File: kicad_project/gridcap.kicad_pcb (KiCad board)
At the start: 2 copper layers, 68 parts

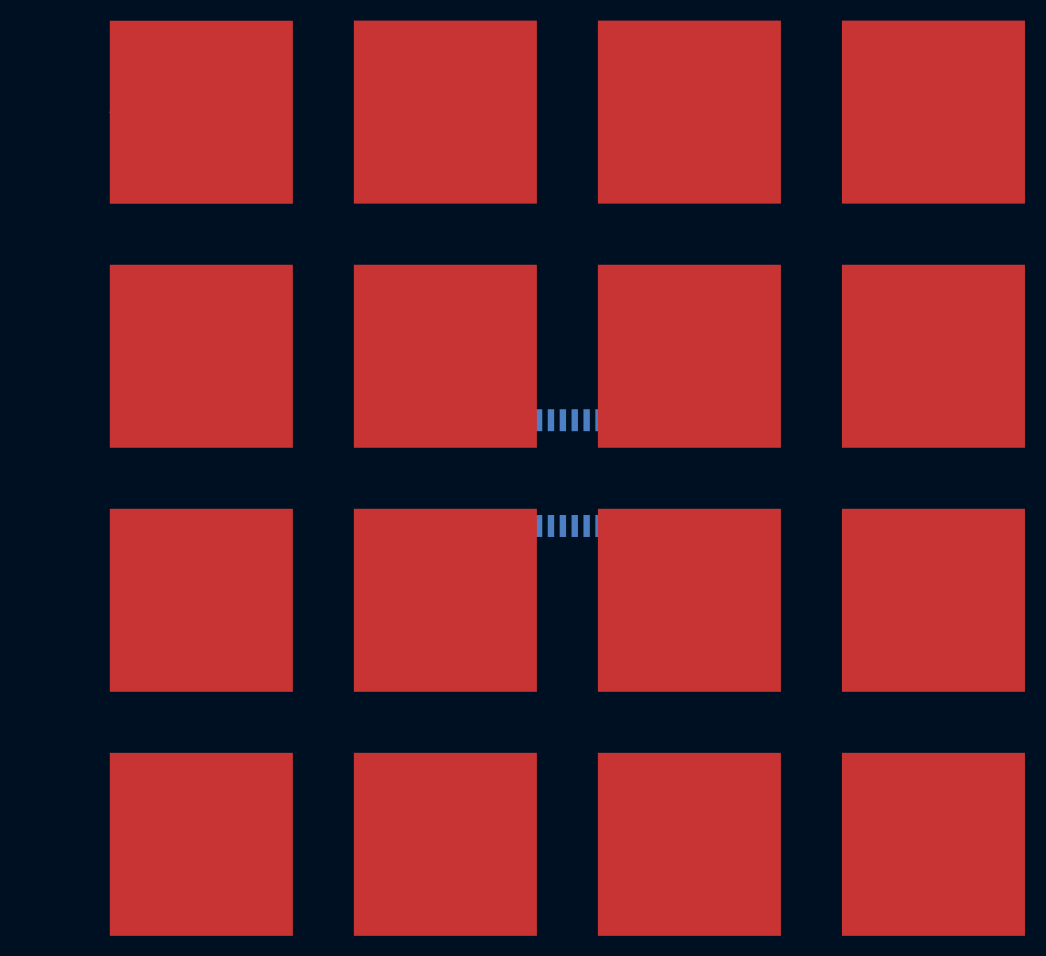
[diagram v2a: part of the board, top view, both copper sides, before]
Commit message: Route one mux on pcb
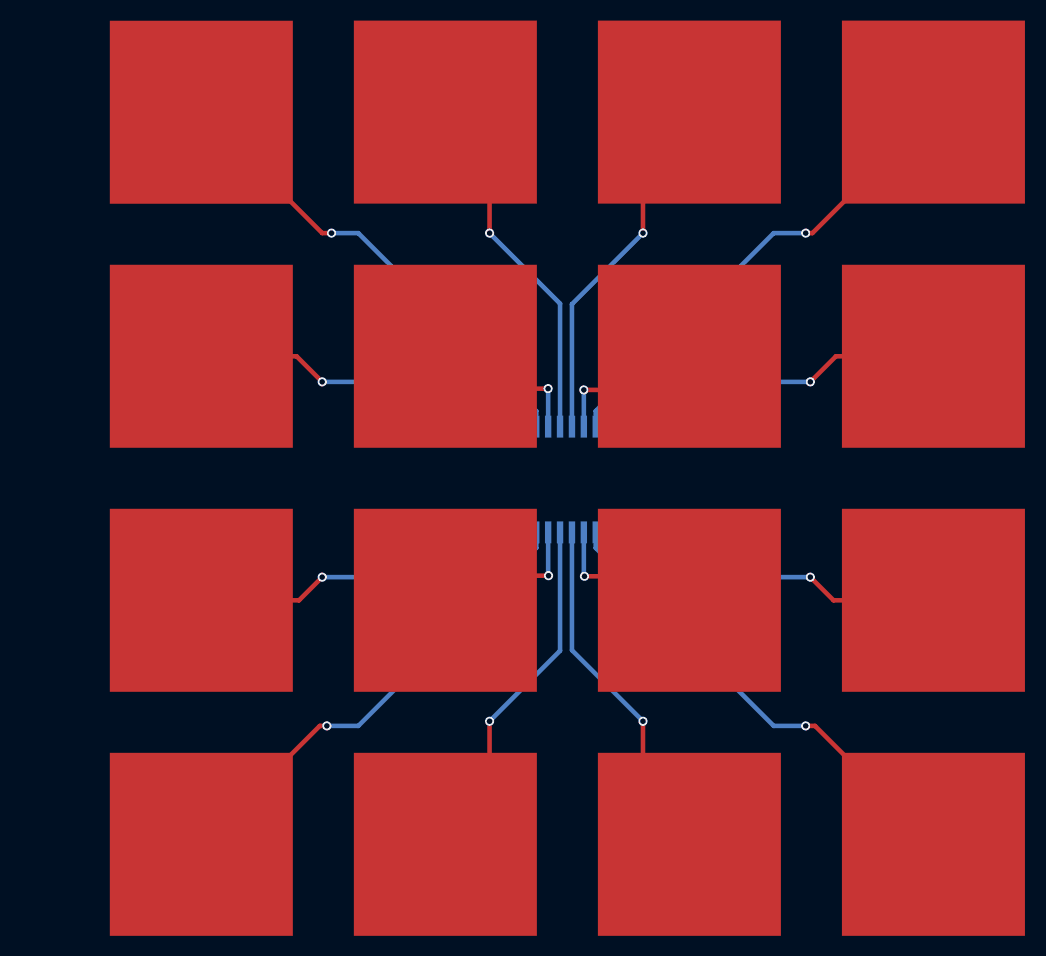
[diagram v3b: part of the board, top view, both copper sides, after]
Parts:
- moved MUX1 0.61 mm to (185.7, 73.4)
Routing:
- net Net-(MUX1-Y1): track 0.00 -> 26.1 mm, vias 0 -> 1
- net Net-(MUX1-Y14): track 0.00 -> 26.0 mm, vias 0 -> 1
- net Net-(MUX1-Y9): track 0.00 -> 25.9 mm, vias 0 -> 1
- net Net-(MUX1-Y6): track 5.00 -> 25.9 mm, vias 0 -> 1
- net Net-(MUX1-Y0): track 0.00 -> 19.9 mm, vias 0 -> 1
- net Net-(MUX1-Y3): track 0.00 -> 19.8 mm, vias 0 -> 1
- net Net-(MUX1-Y15): track 0.00 -> 19.8 mm, vias 0 -> 1
- net Net-(MUX1-Y4): track 0.00 -> 19.8 mm, vias 0 -> 1
- net Net-(MUX1-Y7): track 0.00 -> 19.7 mm, vias 0 -> 1
- net Net-(MUX1-Y12): track 0.00 -> 19.7 mm, vias 0 -> 1
- net Net-(MUX1-Y8): track 0.00 -> 19.7 mm, vias 0 -> 1
- net Net-(MUX1-Y11): track 0.00 -> 19.6 mm, vias 0 -> 1
- net Net-(MUX1-Y13): track 0.00 -> 8.69 mm, vias 0 -> 1
- net Net-(MUX1-Y10): track 0.00 -> 8.57 mm, vias 0 -> 1
- net Net-(MUX1-Y2): track 0.00 -> 8.54 mm, vias 0 -> 1
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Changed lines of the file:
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@@
   )
   (footprint "gridcap_footprints:74HC4067PW-Q100J" (layer "B.Cu")
-    (at 185.177 73.056)
+    (at 185.674 73.406)
     (descr "TSSOP24")
     (property "Sheetfile" "gridcap.kicad_sch")
@@
       (net 122 "unconnected-(MUX1-Vcc-Pad24)") (pinfunction "Vcc") (pintype "power_in") (thermal_bridge_angle 45))
   )
-  (segment (start 165.1 53.34) (end 160.1 53.34) (width 0) (layer "F.Cu") (net 3))
+  (segment (start 170.305 66.673) (end 165.1 66.673) (width 0.25) (layer "F.Cu") (net 2))
+  (segment (start 171.704 68.072) (end 170.305 66.673) (width 0.25) (layer "F.Cu") (net 2))
+  (via (at 171.704 68.072) (size 0.5) (drill 0.3) (layers "F.Cu" "B.Cu") (net 2))
+  (segment (start 182.749 69.666) (end 181.155 68.072) (width 0.25) (layer "B.Cu") (net 2))
+  (segment (start 181.155 68.072) (end 171.704 68.072) (width 0.25) (layer "B.Cu") (net 2))
+  (segment (start 182.749 70.516) (end 182.749 69.666) (width 0.25) (layer "B.Cu") (net 2))
+  (segment (start 171.704 59.944) (end 165.1 53.34) (width 0.25) (layer "F.Cu") (net 3))
+  (segment (start 172.212 59.944) (end 171.704 59.944) (width 0.25) (layer "F.Cu") (net 3))
+  (via (at 172.212 59.944) (size 0.5) (drill 0.3) (layers "F.Cu" "B.Cu") (net 3))
+  (segment (start 183.399 70.516) (end 183.399 69.666) (width 0.25) (layer "B.Cu") (net 3))
+  (segment (start 173.677 59.944) (end 172.212 59.944) (width 0.25) (layer "B.Cu") (net 3))
+  (segment (start 183.399 69.666) (end 173.677 59.944) (width 0.25) (layer "B.Cu") (net 3))
+  (segment (start 184.044991 68.441875) (end 180.201875 68.441875) (width 0.25) (layer "F.Cu") (net 4))
+  (segment (start 180.201875 68.441875) (end 178.433 66.673) (width 0.25) (layer "F.Cu") (net 4))
+  (via (at 184.044991 68.441875) (size 0.5) (drill 0.3) (layers "F.Cu" "B.Cu") (net 4))
+  (segment (start 184.049 68.445884) (end 184.044991 68.441875) (width 0.25) (layer "B.Cu") (net 4))
+  (segment (start 184.049 70.516) (end 184.049 68.445884) (width 0.25) (layer "B.Cu") (net 4))
+  (segment (start 180.848 55.7478) (end 178.433 53.3328) (width 0.25) (layer "F.Cu") (net 5))
+  (segment (start 180.848 59.944) (end 180.848 55.7478) (width 0.25) (layer "F.Cu") (net 5))
+  (via (at 180.848 59.944) (size 0.5) (drill 0.3) (layers "F.Cu" "B.Cu") (net 5))
+  (segment (start 184.699 63.795) (end 180.848 59.944) (width 0.25) (layer "B.Cu") (net 5))
+  (segment (start 184.699 70.516) (end 184.699 63.795) (width 0.25) (layer "B.Cu") (net 5))
+  (segment (start 189.23 55.8688) (end 191.766 53.3328) (width 0.25) (layer "F.Cu") (net 6))
+  (segment (start 189.23 59.944) (end 189.23 55.8688) (width 0.25) (layer "F.Cu") (net 6))
+  (via (at 189.23 59.944) (size 0.5) (drill 0.3) (layers "F.Cu" "B.Cu") (net 6))
+  (segment (start 185.349 63.825) (end 189.23 59.944) (width 0.25) (layer "B.Cu") (net 6))
+  (segment (start 185.349 70.516) (end 185.349 63.825) (width 0.25) (layer "B.Cu") (net 6))
+  (segment (start 189.927805 68.511195) (end 191.766 66.673) (width 0.25) (layer "F.Cu") (net 7))
+  (segment (start 185.997491 68.511195) (end 189.927805 68.511195) (width 0.25) (layer "F.Cu") (net 7))
+  (via (at 185.997491 68.511195) (size 0.5) (drill 0.3) (layers "F.Cu" "B.Cu") (net 7))
+  (segment (start 185.999 68.512704) (end 185.997491 68.511195) (width 0.25) (layer "B.Cu") (net 7))
+  (segment (start 185.999 70.516) (end 185.999 68.512704) (width 0.25) (layer "B.Cu") (net 7))
+  (segment (start 198.4878 59.944) (end 205.099 53.3328) (width 0.25) (layer "F.Cu") (net 8))
+  (segment (start 198.12 59.944) (end 198.4878 59.944) (width 0.25) (layer "F.Cu") (net 8))
+  (via (at 198.12 59.944) (size 0.5) (drill 0.3) (layers "F.Cu" "B.Cu") (net 8))
+  (segment (start 196.371 59.944) (end 198.12 59.944) (width 0.25) (layer "B.Cu") (net 8))
+  (segment (start 186.649 69.666) (end 196.371 59.944) (width 0.25) (layer "B.Cu") (net 8))
+  (segment (start 186.649 70.516) (end 186.649 69.666) (width 0.25) (layer "B.Cu") (net 8))
+  (segment (start 199.773 66.673) (end 205.099 66.673) (width 0.25) (layer "F.Cu") (net 9))
+  (segment (start 198.374 68.072) (end 199.773 66.673) (width 0.25) (layer "F.Cu") (net 9))
+  (via (at 198.374 68.072) (size 0.5) (drill 0.3) (layers "F.Cu" "B.Cu") (net 9))
+  (segment (start 187.299 69.666) (end 188.893 68.072) (width 0.25) (layer "B.Cu") (net 9))
+  (segment (start 188.893 68.072) (end 198.374 68.072) (width 0.25) (layer "B.Cu") (net 9))
+  (segment (start 187.299 70.516) (end 187.299 69.666) (width 0.25) (layer "B.Cu") (net 9))
+  (segment (start 199.64 80.006) (end 205.099 80.006) (width 0.25) (layer "F.Cu") (net 15))
+  (segment (start 198.374 78.74) (end 199.64 80.006) (width 0.25) (layer "F.Cu") (net 15))
+  (via (at 198.374 78.74) (size 0.5) (drill 0.3) (layers "F.Cu" "B.Cu") (net 15))
+  (segment (start 188.893 78.74) (end 198.374 78.74) (width 0.25) (layer "B.Cu") (net 15))
+  (segment (start 187.299 77.146) (end 188.893 78.74) (width 0.25) (layer "B.Cu") (net 15))
+  (segment (start 187.299 76.296) (end 187.299 77.146) (width 0.25) (layer "B.Cu") (net 15))
+  (segment (start 198.628 86.868) (end 205.099 93.339) (width 0.25) (layer "F.Cu") (net 16))
+  (segment (start 198.12 86.868) (end 198.628 86.868) (width 0.25) (layer "F.Cu") (net 16))
+  (via (at 198.12 86.868) (size 0.5) (drill 0.3) (layers "F.Cu" "B.Cu") (net 16))
+  (segment (start 196.371 86.868) (end 198.12 86.868) (width 0.25) (layer "B.Cu") (net 16))
+  (segment (start 186.649 76.296) (end 186.649 77.146) (width 0.25) (layer "B.Cu") (net 16))
+  (segment (start 186.649 77.146) (end 196.371 86.868) (width 0.25) (layer "B.Cu") (net 16))
+  (segment (start 190.454046 78.694046) (end 191.766 80.006) (width 0.25) (layer "F.Cu") (net 17))
+  (segment (start 186.033179 78.694046) (end 190.454046 78.694046) (width 0.25) (layer "F.Cu") (net 17))
+  (via (at 186.033179 78.694046) (size 0.5) (drill 0.3) (layers "F.Cu" "B.Cu") (net 17))
+  (segment (start 185.999 78.659867) (end 186.033179 78.694046) (width 0.25) (layer "B.Cu") (net 17))
+  (segment (start 185.999 76.296) (end 185.999 78.659867) (width 0.25) (layer "B.Cu") (net 17))
+  (segment (start 189.23 90.803) (end 191.766 93.339) (width 0.25) (layer "F.Cu") (net 18))
+  (segment (start 189.23 86.614) (end 189.23 90.803) (width 0.25) (layer "F.Cu") (net 18))
+  (via (at 189.23 86.614) (size 0.5) (drill 0.3) (layers "F.Cu" "B.Cu") (net 18))
+  (segment (start 185.349 82.733) (end 189.23 86.614) (width 0.25) (layer "B.Cu") (net 18))
+  (segment (start 185.349 76.296) (end 185.349 82.733) (width 0.25) (layer "B.Cu") (net 18))
+  (segment (start 180.848 86.614) (end 180.848 90.924) (width 0.25) (layer "F.Cu") (net 19))
+  (segment (start 180.848 90.924) (end 178.433 93.339) (width 0.25) (layer "F.Cu") (net 19))
+  (via (at 180.848 86.614) (size 0.5) (drill 0.3) (layers "F.Cu" "B.Cu") (net 19))
+  (segment (start 184.699 76.296) (end 184.699 82.763) (width 0.25) (layer "B.Cu") (net 19))
+  (segment (start 184.699 82.763) (end 180.848 86.614) (width 0.25) (layer "B.Cu") (net 19))
+  (segment (start 179.778857 78.660143) (end 178.433 80.006) (width 0.25) (layer "F.Cu") (net 20))
+  (segment (start 184.070143 78.660143) (end 179.778857 78.660143) (width 0.25) (layer "F.Cu") (net 20))
+  (via (at 184.070143 78.660143) (size 0.5) (drill 0.3) (layers "F.Cu" "B.Cu") (net 20))
+  (segment (start 184.049 76.296) (end 184.049 78.639) (width 0.25) (layer "B.Cu") (net 20))
+  (segment (start 184.049 78.639) (end 184.070143 78.660143) (width 0.25) (layer "B.Cu") (net 20))
+  (segment (start 171.958 86.868) (end 171.571 86.868) (width 0.25) (layer "F.Cu") (net 21))
+  (segment (start 171.571 86.868) (end 165.1 93.339) (width 0.25) (layer "F.Cu") (net 21))
+  (via (at 171.958 86.868) (size 0.5) (drill 0.3) (layers "F.Cu" "B.Cu") (net 21))
+  (segment (start 183.399 77.146) (end 173.677 86.868) (width 0.25) (layer "B.Cu") (net 21))
+  (segment (start 183.399 76.296) (end 183.399 77.146) (width 0.25) (layer "B.Cu") (net 21))
+  (segment (start 173.677 86.868) (end 171.958 86.868) (width 0.25) (layer "B.Cu") (net 21))
+  (segment (start 171.704 78.74) (end 170.438 80.006) (width 0.25) (layer "F.Cu") (net 22))
+  (segment (start 170.438 80.006) (end 165.1 80.006) (width 0.25) (layer "F.Cu") (net 22))
+  (via (at 171.704 78.74) (size 0.5) (drill 0.3) (layers "F.Cu" "B.Cu") (net 22))
+  (segment (start 182.749 76.296) (end 182.749 77.146) (width 0.25) (layer "B.Cu") (net 22))
+  (segment (start 182.749 77.146) (end 181.155 78.74) (width 0.25) (layer "B.Cu") (net 22))
+  (segment (start 181.155 78.74) (end 171.704 78.74) (width 0.25) (layer "B.Cu") (net 22))
 )

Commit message: Route all muxes to pads
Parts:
- MUX4: moved to B.Cu
- moved MUX4 139.9 mm to (239.1, 126.7), turned to 0 degrees
- moved MUX2 131.7 mm to (239.1, 73.4)
- moved MUX3 97.3 mm to (185.7, 126.7)
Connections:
- MUX2 pad 16: unconnected-(MUX2-Y15-Pad16) -> Net-(MUX2-Y15)
- MUX2 pad 17: unconnected-(MUX2-Y14-Pad17) -> Net-(MUX2-Y14)
- MUX2 pad 18: unconnected-(MUX2-Y13-Pad18) -> Net-(MUX2-Y13)
- MUX2 pad 19: unconnected-(MUX2-Y12-Pad19) -> Net-(MUX2-Y12)
- MUX2 pad 2: unconnected-(MUX2-Y7-Pad2) -> Net-(MUX2-Y7)
- MUX2 pad 20: unconnected-(MUX2-Y11-Pad20) -> Net-(MUX2-Y11)
- MUX2 pad 21: unconnected-(MUX2-Y10-Pad21) -> Net-(MUX2-Y10)
- MUX2 pad 22: unconnected-(MUX2-Y9-Pad22) -> Net-(MUX2-Y9)
- MUX2 pad 23: unconnected-(MUX2-Y8-Pad23) -> Net-(MUX2-Y8)
- MUX2 pad 3: unconnected-(MUX2-Y6-Pad3) -> Net-(MUX2-Y6)
- MUX2 pad 4: unconnected-(MUX2-Y5-Pad4) -> Net-(MUX2-Y5)
- MUX2 pad 5: unconnected-(MUX2-Y4-Pad5) -> Net-(MUX2-Y4)
- MUX2 pad 6: unconnected-(MUX2-Y3-Pad6) -> Net-(MUX2-Y3)
- MUX2 pad 7: unconnected-(MUX2-Y2-Pad7) -> Net-(MUX2-Y2)
- MUX2 pad 8: unconnected-(MUX2-Y1-Pad8) -> Net-(MUX2-Y1)
- MUX2 pad 9: unconnected-(MUX2-Y0-Pad9) -> Net-(MUX2-Y0)
- MUX3 pad 16: unconnected-(MUX3-Y15-Pad16) -> Net-(MUX3-Y15)
- MUX3 pad 17: unconnected-(MUX3-Y14-Pad17) -> Net-(MUX3-Y14)
- MUX3 pad 18: unconnected-(MUX3-Y13-Pad18) -> Net-(MUX3-Y13)
- MUX3 pad 19: unconnected-(MUX3-Y12-Pad19) -> Net-(MUX3-Y12)
- MUX3 pad 2: unconnected-(MUX3-Y7-Pad2) -> Net-(MUX3-Y7)
- MUX3 pad 20: unconnected-(MUX3-Y11-Pad20) -> Net-(MUX3-Y11)
- MUX3 pad 21: unconnected-(MUX3-Y10-Pad21) -> Net-(MUX3-Y10)
- MUX3 pad 22: unconnected-(MUX3-Y9-Pad22) -> Net-(MUX3-Y9)
- MUX3 pad 23: unconnected-(MUX3-Y8-Pad23) -> Net-(MUX3-Y8)
- MUX3 pad 3: unconnected-(MUX3-Y6-Pad3) -> Net-(MUX3-Y6)
- MUX3 pad 4: unconnected-(MUX3-Y5-Pad4) -> Net-(MUX3-Y5)
- MUX3 pad 5: unconnected-(MUX3-Y4-Pad5) -> Net-(MUX3-Y4)
- MUX3 pad 6: unconnected-(MUX3-Y3-Pad6) -> Net-(MUX3-Y3)
- MUX3 pad 7: unconnected-(MUX3-Y2-Pad7) -> Net-(MUX3-Y2)
- MUX3 pad 8: unconnected-(MUX3-Y1-Pad8) -> Net-(MUX3-Y1)
- MUX3 pad 9: unconnected-(MUX3-Y0-Pad9) -> Net-(MUX3-Y0)
- MUX4 pad 16: unconnected-(MUX4-Y15-Pad16) -> Net-(MUX4-Y15)
- MUX4 pad 17: unconnected-(MUX4-Y14-Pad17) -> Net-(MUX4-Y14)
- MUX4 pad 18: unconnected-(MUX4-Y13-Pad18) -> Net-(MUX4-Y13)
- MUX4 pad 19: unconnected-(MUX4-Y12-Pad19) -> Net-(MUX4-Y12)
- MUX4 pad 2: unconnected-(MUX4-Y7-Pad2) -> Net-(MUX4-Y7)
- MUX4 pad 20: unconnected-(MUX4-Y11-Pad20) -> Net-(MUX4-Y11)
- MUX4 pad 21: unconnected-(MUX4-Y10-Pad21) -> Net-(MUX4-Y10)
- MUX4 pad 22: unconnected-(MUX4-Y9-Pad22) -> Net-(MUX4-Y9)
- MUX4 pad 23: unconnected-(MUX4-Y8-Pad23) -> Net-(MUX4-Y8)
- MUX4 pad 3: unconnected-(MUX4-Y6-Pad3) -> Net-(MUX4-Y6)
- MUX4 pad 4: unconnected-(MUX4-Y5-Pad4) -> Net-(MUX4-Y5)
- MUX4 pad 5: unconnected-(MUX4-Y4-Pad5) -> Net-(MUX4-Y4)
- MUX4 pad 6: unconnected-(MUX4-Y3-Pad6) -> Net-(MUX4-Y3)
- MUX4 pad 7: unconnected-(MUX4-Y2-Pad7) -> Net-(MUX4-Y2)
- MUX4 pad 8: unconnected-(MUX4-Y1-Pad8) -> Net-(MUX4-Y1)
- MUX4 pad 9: unconnected-(MUX4-Y0-Pad9) -> Net-(MUX4-Y0)
- PAD13 pad 1: unconnected-(PAD13-Pad1) -> Net-(MUX2-Y7)
- PAD14 pad 1: unconnected-(PAD14-Pad1) -> Net-(MUX2-Y5)
- PAD15 pad 1: unconnected-(PAD15-Pad1) -> Net-(MUX2-Y2)
- PAD16 pad 1: unconnected-(PAD16-Pad1) -> Net-(MUX2-Y0)
- PAD21 pad 1: unconnected-(PAD21-Pad1) -> Net-(MUX2-Y8)
- PAD22 pad 1: unconnected-(PAD22-Pad1) -> Net-(MUX2-Y10)
- PAD23 pad 1: unconnected-(PAD23-Pad1) -> Net-(MUX2-Y13)
- PAD24 pad 1: unconnected-(PAD24-Pad1) -> Net-(MUX2-Y15)
- PAD29 pad 1: unconnected-(PAD29-Pad1) -> Net-(MUX2-Y9)
- PAD30 pad 1: unconnected-(PAD30-Pad1) -> Net-(MUX2-Y11)
- PAD31 pad 1: unconnected-(PAD31-Pad1) -> Net-(MUX2-Y12)
- PAD32 pad 1: unconnected-(PAD32-Pad1) -> Net-(MUX2-Y14)
- PAD33 pad 1: unconnected-(PAD33-Pad1) -> Net-(MUX3-Y6)
- PAD34 pad 1: unconnected-(PAD34-Pad1) -> Net-(MUX3-Y4)
- PAD35 pad 1: unconnected-(PAD35-Pad1) -> Net-(MUX3-Y3)
- PAD36 pad 1: unconnected-(PAD36-Pad1) -> Net-(MUX3-Y1)
- PAD37 pad 1: unconnected-(PAD37-Pad1) -> Net-(MUX4-Y6)
- PAD38 pad 1: unconnected-(PAD38-Pad1) -> Net-(MUX4-Y4)
- PAD39 pad 1: unconnected-(PAD39-Pad1) -> Net-(MUX4-Y3)
- PAD40 pad 1: unconnected-(PAD40-Pad1) -> Net-(MUX4-Y1)
- PAD41 pad 1: unconnected-(PAD41-Pad1) -> Net-(MUX3-Y7)
- PAD42 pad 1: unconnected-(PAD42-Pad1) -> Net-(MUX3-Y5)
- PAD43 pad 1: unconnected-(PAD43-Pad1) -> Net-(MUX3-Y2)
- PAD44 pad 1: unconnected-(PAD44-Pad1) -> Net-(MUX3-Y0)
- PAD45 pad 1: unconnected-(PAD45-Pad1) -> Net-(MUX4-Y7)
- PAD46 pad 1: unconnected-(PAD46-Pad1) -> Net-(MUX4-Y5)
- PAD47 pad 1: unconnected-(PAD47-Pad1) -> Net-(MUX4-Y2)
- PAD48 pad 1: unconnected-(PAD48-Pad1) -> Net-(MUX4-Y0)
- PAD49 pad 1: unconnected-(PAD49-Pad1) -> Net-(MUX3-Y8)
- PAD5 pad 1: unconnected-(PAD5-Pad1) -> Net-(MUX2-Y6)
- PAD50 pad 1: unconnected-(PAD50-Pad1) -> Net-(MUX3-Y10)
- PAD51 pad 1: unconnected-(PAD51-Pad1) -> Net-(MUX3-Y13)
- PAD52 pad 1: unconnected-(PAD52-Pad1) -> Net-(MUX3-Y15)
- PAD53 pad 1: unconnected-(PAD53-Pad1) -> Net-(MUX4-Y8)
- PAD54 pad 1: unconnected-(PAD54-Pad1) -> Net-(MUX4-Y10)
- PAD55 pad 1: unconnected-(PAD55-Pad1) -> Net-(MUX4-Y13)
- PAD56 pad 1: unconnected-(PAD56-Pad1) -> Net-(MUX4-Y15)
- PAD57 pad 1: unconnected-(PAD57-Pad1) -> Net-(MUX3-Y9)
- PAD58 pad 1: unconnected-(PAD58-Pad1) -> Net-(MUX3-Y11)
- PAD59 pad 1: unconnected-(PAD59-Pad1) -> Net-(MUX3-Y12)
- PAD6 pad 1: unconnected-(PAD6-Pad1) -> Net-(MUX2-Y4)
- PAD60 pad 1: unconnected-(PAD60-Pad1) -> Net-(MUX3-Y14)
- PAD61 pad 1: unconnected-(PAD61-Pad1) -> Net-(MUX4-Y9)
- PAD62 pad 1: unconnected-(PAD62-Pad1) -> Net-(MUX4-Y11)
- PAD63 pad 1: unconnected-(PAD63-Pad1) -> Net-(MUX4-Y12)
- PAD64 pad 1: unconnected-(PAD64-Pad1) -> Net-(MUX4-Y14)
- PAD7 pad 1: unconnected-(PAD7-Pad1) -> Net-(MUX2-Y3)
- PAD8 pad 1: unconnected-(PAD8-Pad1) -> Net-(MUX2-Y1)
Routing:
- net Net-(MUX2-Y1): track 0.00 -> 26.0 mm, vias 0 -> 1
- net Net-(MUX3-Y1): track 0.00 -> 26.0 mm, vias 0 -> 1
- net Net-(MUX2-Y14): track 0.00 -> 26.0 mm, vias 0 -> 1
- net Net-(MUX4-Y14): track 0.00 -> 26.0 mm, vias 0 -> 1
- net Net-(MUX4-Y1): track 0.00 -> 26.0 mm, vias 0 -> 1
- net Net-(MUX3-Y6): track 0.00 -> 26.0 mm, vias 0 -> 1
- net Net-(MUX3-Y14): track 0.00 -> 26.0 mm, vias 0 -> 1
- net Net-(MUX4-Y9): track 0.00 -> 26.0 mm, vias 0 -> 1
- net Net-(MUX2-Y6): track 0.00 -> 25.9 mm, vias 0 -> 1
- net Net-(MUX4-Y6): track 0.00 -> 25.9 mm, vias 0 -> 1
- net Net-(MUX3-Y9): track 0.00 -> 25.9 mm, vias 0 -> 1
- net Net-(MUX2-Y9): track 0.00 -> 25.9 mm, vias 0 -> 1
- net Net-(MUX2-Y0): track 0.00 -> 19.8 mm, vias 0 -> 1
- net Net-(MUX3-Y0): track 0.00 -> 19.8 mm, vias 0 -> 1
- net Net-(MUX2-Y15): track 0.00 -> 19.8 mm, vias 0 -> 1
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
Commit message: Route all muxes and add pcb shape
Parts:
- added J1: Conn_01x10, Connector_PinHeader_2.54mm:PinHeader_1x10_P2.54mm_Vertical, F.Cu at (151.4, 111.5)
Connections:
- MUX1 pad 24: unconnected-(MUX1-Vcc-Pad24) -> Vcc
- MUX2 pad 24: unconnected-(MUX2-Vcc-Pad24) -> Vcc
- MUX3 pad 24: unconnected-(MUX3-Vcc-Pad24) -> Vcc
- MUX4 pad 24: unconnected-(MUX4-Vcc-Pad24) -> Vcc
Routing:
- net Vcc: track 0.00 -> 262.4 mm, vias 0 -> 6
- net S2: track 0.00 -> 228.0 mm, vias 0 -> 3
- net S3: track 0.00 -> 225.8 mm, vias 0 -> 2
- net S0: track 0.00 -> 224.8 mm, vias 0 -> 4
- net S1: track 0.00 -> 223.3 mm, vias 0 -> 4
- net Z2: track 0.00 -> 101.4 mm, vias 0 -> 2
- net Z4: track 0.00 -> 100.8 mm, vias 0 -> 1
- net Z1: track 0.00 -> 56.7 mm, vias 0 -> 2
- net Z3: track 0.00 -> 48.1 mm, vias 0 -> 1
- net GND: track 0.00 -> 15.2 mm, vias 0 -> 4
- net Net-(MUX1-Y15): track 19.8 -> 22.8 mm
- net Net-(MUX2-Y8): track 19.8 -> 21.1 mm
- added copper zone on B.Cu, net GND
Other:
- board outline added: 119.1 x 108.7 mm
